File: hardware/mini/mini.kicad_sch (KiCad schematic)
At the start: 12 parts, among them J1 Conn_01x03, J2 Conn_02x05_Odd_Even, J3 Conn_02x05_Odd_Even

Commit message: route power stage
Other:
- sheet channel_A ports: added CONVERTER_~{INT}, SENSE_~{INT}; removed SENSE_INT
- sheet channel_B ports: added CONVERTER_~{INT}, SENSE_~{INT}; removed SENSE_INT
- sheet interface ports: added COL_2; removed ROW_3, ROW_4
- sheet mcu ports: added COL_2, CONVERTER_INT_A, CONVERTER_INT_B; removed ROW_3, ROW_4

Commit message: route
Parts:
- added N2: Breadboard, symbol Mechanical:Housing
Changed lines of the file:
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@@
+	)
+	(symbol
+		(lib_id "Mechanical:Housing")
+		(at 182.88 156.21 0)
+		(unit 1)
+		(exclude_from_sim no)
+		(in_bom yes)
+		(on_board yes)
+		(dnp no)
+		(fields_autoplaced yes)
+		(property "Reference" "N2"
+			(at 186.69 155.2574 0)
+			(effects
+				(font
+					(size 1.27 1.27)
+				)
+				(justify left)
+			)
+		)
+		(property "Value" "Breadboard"
+			(at 186.69 157.7974 0)
+			(effects
+				(font
+					(size 1.27 1.27)
+				)
+				(justify left)
+			)
+		)
+		(property "Footprint" ""
+			(at 184.15 154.94 0)
+			(effects
+				(font
+					(size 1.27 1.27)
+				)
+				(hide yes)
+			)
+		)
+		(property "Datasheet" "~"
+			(at 184.15 154.94 0)
+			(effects
+				(font
+					(size 1.27 1.27)
+				)
+				(hide yes)
+			)
+		)
+		(property "Description" "Housing"
+			(at 182.88 156.21 0)
+			(effects
+				(font
+					(size 1.27 1.27)
+				)
+				(hide yes)
+			)
+		)
+		(instances
+			(project ""
+				(path "/5aaaac9a-5acd-4aef-ad51-a6d04aa88705"
+					(reference "N2")
+					(unit 1)
+				)
+			)
+		)
 	)
 	(symbol

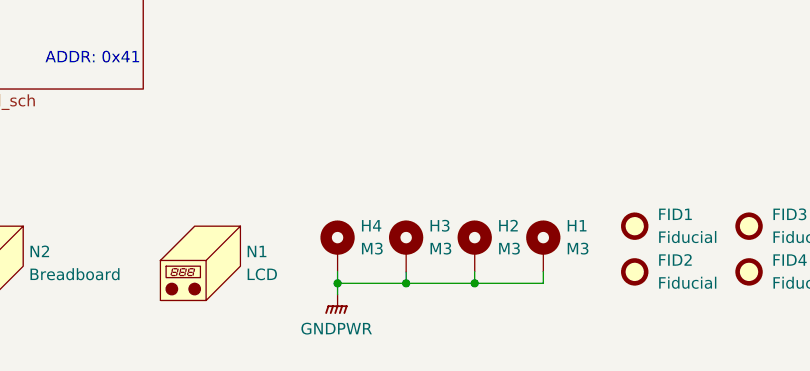
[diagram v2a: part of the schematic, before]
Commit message: route digitals
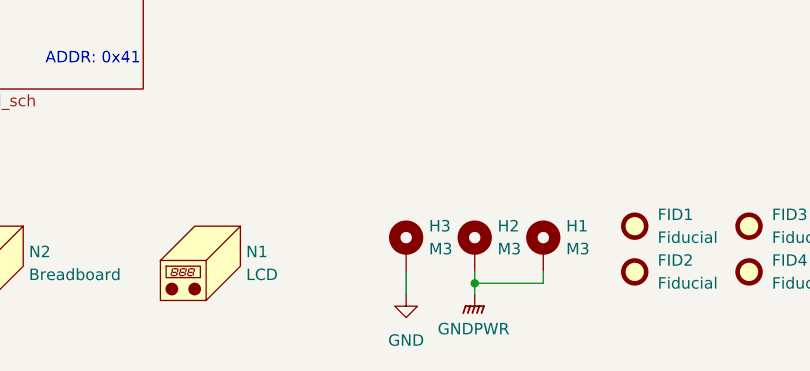
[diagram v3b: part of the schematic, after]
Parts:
- removed H4: M3, MountingHole:MountingHole_3.2mm_M3_DIN965_Pad_TopBottom, symbol Mechanical:MountingHole_Pad
- N2: footprint (none) -> protovolt_mini_fp:Breadboard_400P
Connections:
- net GND: now also H3.1
- net GNDPWR: no longer H3.1

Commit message: reroute all except 3V3 & GND
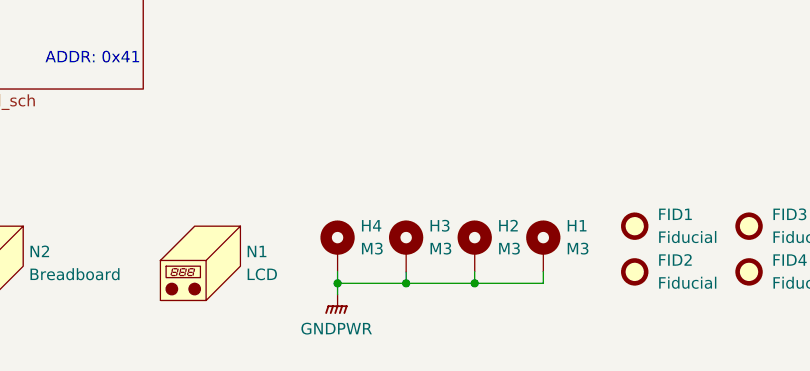
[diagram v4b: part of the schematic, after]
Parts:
- added H4: M3, MountingHole:MountingHole_3.2mm_M3_DIN965_Pad_TopBottom, symbol Mechanical:MountingHole_Pad
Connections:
- net GND: no longer H3.1
- net GNDPWR: now also H3.1, H4.1
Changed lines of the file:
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@@
+	)
+	(junction
+		(at 220.98 158.75)
+		(diameter 0)
+		(color 0 0 0 0)
 	)
 	(junction
@@
 	)
 	(junction
+		(at 228.6 158.75)
+		(diameter 0)
+		(color 0 0 0 0)
+	)
+	(junction
 		(at 236.22 55.88)
 		(diameter 0)
@@
 	(wire
 		(pts
-			(xy 228.6 157.48) (xy 228.6 160.02)
-		)
-		(stroke
-			(width 0)
-			(type default)
-		)
-	)
-	(wire
-		(pts
-			(xy 236.22 158.75) (xy 236.22 160.02)
+			(xy 220.98 158.75) (xy 220.98 160.02)
 		)
 		(stroke
@@
 	(wire
 		(pts
+			(xy 228.6 157.48) (xy 228.6 158.75)
+		)
+		(stroke
+			(width 0)
+			(type default)
+		)
+	)
+	(wire
+		(pts
+			(xy 220.98 158.75) (xy 228.6 158.75)
+		)
+		(stroke
+			(width 0)
+			(type default)
+		)
+	)
+	(wire
+		(pts
 			(xy 168.91 125.73) (xy 152.4 125.73)
 		)
@@
 	(wire
 		(pts
+			(xy 220.98 157.48) (xy 220.98 158.75)
+		)
+		(stroke
+			(width 0)
+			(type default)
+		)
+	)
+	(wire
+		(pts
 			(xy 90.17 49.53) (xy 102.87 49.53)
 		)
@@
 		(pts
 			(xy 90.17 63.5) (xy 96.52 63.5)
+		)
+		(stroke
+			(width 0)
+			(type default)
+		)
+	)
+	(wire
+		(pts
+			(xy 228.6 158.75) (xy 236.22 158.75)
 		)
 		(stroke
@@
 	(symbol
 		(lib_id "Mechanical:MountingHole_Pad")
+		(at 220.98 154.94 0)
+		(unit 1)
+		(exclude_from_sim no)
+		(in_bom no)
+		(on_board yes)
+		(dnp no)
+		(fields_autoplaced yes)
+		(property "Reference" "H4"
+			(at 223.52 152.3999 0)
+			(effects
+				(font
+					(size 1.27 1.27)
+				)
+				(justify left)
+			)
+		)
+		(property "Value" "M3"
+			(at 223.52 154.9399 0)
+			(effects
+				(font
+					(size 1.27 1.27)
+				)
+				(justify left)
+			)
+		)
+		(property "Footprint" "MountingHole:MountingHole_3.2mm_M3_DIN965_Pad_TopBottom"
+			(at 220.98 154.94 0)
+			(effects
+				(font
+					(size 1.27 1.27)
+				)
+				(hide yes)
+			)
+		)
+		(property "Datasheet" "~"
+			(at 220.98 154.94 0)
+			(effects
+				(font
+					(size 1.27 1.27)
+				)
+				(hide yes)
+			)
+		)
+		(property "Description" "Mounting Hole with connection"
+			(at 220.98 154.94 0)
+			(effects
+				(font
+					(size 1.27 1.27)
+				)
+				(hide yes)
+			)
+		)
+		(pin "1"
+		)
+		(instances
+			(project "mini"
+				(path "/5aaaac9a-5acd-4aef-ad51-a6d04aa88705"
+					(reference "H4")
+					(unit 1)
+				)
+			)
+		)
+	)
+	(symbol
+		(lib_id "Mechanical:MountingHole_Pad")
 		(at 236.22 154.94 0)
 		(unit 1)
@@
 	(symbol
 		(lib_id "power:GNDPWR")
-		(at 236.22 160.02 0)
+		(at 220.98 160.02 0)
 		(unit 1)
 		(exclude_from_sim no)
@@
 		(fields_autoplaced yes)
 		(property "Reference" "#PWR0123"
-			(at 236.22 165.1 0)
+			(at 220.98 165.1 0)
 			(effects
 				(font
@@
 		)
 		(property "Value" "GNDPWR"
-			(at 236.093 163.83 0)
+			(at 220.853 163.83 0)
 			(effects
 				(font
@@
 		)
 		(property "Footprint" ""
-			(at 236.22 161.29 0)
+			(at 220.98 161.29 0)
 			(effects
 				(font
@@
 		)
 		(property "Datasheet" ""
-			(at 236.22 161.29 0)
+			(at 220.98 161.29 0)
 			(effects
 				(font
@@
 		)
 		(property "Description" "Power symbol creates a global label with name \"GNDPWR\" , global ground"
-			(at 236.22 160.02 0)
+			(at 220.98 160.02 0)
 			(effects
 				(font
@@
 					(unit 1)
 				)
-			)
-		)
-	)
-	(symbol
-		(lib_id "power:GND")
-		(at 228.6 160.02 0)
-		(unit 1)
-		(exclude_from_sim no)
-		(in_bom yes)
-		(on_board yes)
-		(dnp no)
-		(fields_autoplaced yes)
-		(property "Reference" "#PWR057"
-			(at 228.6 166.37 0)
-			(effects
-				(font
-					(size 1.27 1.27)
-				)
-				(hide yes)
-			)
-		)
-		(property "Value" "GND"
-			(at 228.6 165.1 0)
-			(effects
-				(font
-					(size 1.27 1.27)
-				)
-			)
-		)
-		(property "Footprint" ""
-			(at 228.6 160.02 0)
-			(effects
-				(font
-					(size 1.27 1.27)
-				)
-				(hide yes)
-			)
-		)
-		(property "Datasheet" ""
-			(at 228.6 160.02 0)
-			(effects
-				(font
-					(size 1.27 1.27)
-				)
-				(hide yes)
-			)
-		)
-		(property "Description" "Power symbol creates a global label with name \"GND\" , ground"
-			(at 228.6 160.02 0)
-			(effects
-				(font
-					(size 1.27 1.27)
-				)
-				(hide yes)
-			)
-		)
-		(pin "1"
-		)
-		(instances
-			(project ""
-				(path "/5aaaac9a-5acd-4aef-ad51-a6d04aa88705"
-					(reference "#PWR057")
-					(unit 1)
-				)

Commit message: finish routing
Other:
- sheet channel_A ports: added GNDA; removed none
- sheet channel_B ports: added GNDA; removed none
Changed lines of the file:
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@@
+	(wire
+		(pts
+			(xy 201.93 86.36) (xy 201.93 88.9)
+		)
+		(stroke
+			(width 0)
+			(type default)
+		)
+	)
 	(wire
 		(pts
@@
 	(wire
 		(pts
+			(xy 199.39 135.89) (xy 201.93 135.89)
+		)
+		(stroke
+			(width 0)
+			(type default)
+		)
+	)
+	(wire
+		(pts
 			(xy 90.17 69.85) (xy 102.87 69.85)
 		)
@@
 	(wire
 		(pts
+			(xy 201.93 135.89) (xy 201.93 138.43)
+		)
+		(stroke
+			(width 0)
+			(type default)
+		)
+	)
+	(wire
+		(pts
 			(xy 236.22 50.8) (xy 236.22 53.34)
 		)
@@
 		(pts
 			(xy 168.91 128.27) (xy 151.13 128.27)
+		)
+		(stroke
+			(width 0)
+			(type default)
+		)
+	)
+	(wire
+		(pts
+			(xy 199.39 86.36) (xy 201.93 86.36)
 		)
 		(stroke
@@
 	)
 	(symbol
+		(lib_id "power:GND2")
+		(at 201.93 138.43 0)
+		(unit 1)
+		(exclude_from_sim no)
+		(in_bom yes)
+		(on_board yes)
+		(dnp no)
+		(fields_autoplaced yes)
+		(property "Reference" "#PWR013"
+			(at 201.93 144.78 0)
+			(effects
+				(font
+					(size 1.27 1.27)
+				)
+				(hide yes)
+			)
+		)
+		(property "Value" "GND2"
+			(at 201.93 143.51 0)
+			(effects
+				(font
+					(size 1.27 1.27)
+				)
+			)
+		)
+		(property "Footprint" ""
+			(at 201.93 138.43 0)
+			(effects
+				(font
+					(size 1.27 1.27)
+				)
+				(hide yes)
+			)
+		)
+		(property "Datasheet" ""
+			(at 201.93 138.43 0)
+			(effects
+				(font
+					(size 1.27 1.27)
+				)
+				(hide yes)
+			)
+		)
+		(property "Description" "Power symbol creates a global label with name \"GND2\" , ground"
+			(at 201.93 138.43 0)
+			(effects
+				(font
+					(size 1.27 1.27)
+				)
+				(hide yes)
+			)
+		)
+		(pin "1"
+		)
+		(instances
+			(project ""
+				(path "/5aaaac9a-5acd-4aef-ad51-a6d04aa88705"
+					(reference "#PWR013")
+					(unit 1)
+				)
+			)
+		)
+	)
+	(symbol
 		(lib_id "power:GNDPWR")
 		(at 236.22 113.03 0)
@@
 				(path "/5aaaac9a-5acd-4aef-ad51-a6d04aa88705"
 					(reference "#PWR07")
+					(unit 1)
+				)
+			)
+		)
+	)
+	(symbol
+		(lib_id "power:GND2")
+		(at 166.37 121.92 270)
+		(unit 1)
+		(exclude_from_sim no)
+		(in_bom yes)
+		(on_board yes)
+		(dnp no)
+		(fields_autoplaced yes)
+		(property "Reference" "#PWR04"
+			(at 160.02 121.92 0)
+			(effects
+				(font
+					(size 1.27 1.27)
+				)
+				(hide yes)
+			)
+		)
+		(property "Value" "GND2"
+			(at 162.56 121.9199 90)
+			(effects
+				(font
+					(size 1.27 1.27)
+				)
+				(justify right)
+			)
+		)
+		(property "Footprint" ""
+			(at 166.37 121.92 0)
+			(effects
+				(font
+					(size 1.27 1.27)
+				)
+				(hide yes)
+			)
+		)
+		(property "Datasheet" ""
+			(at 166.37 121.92 0)
+			(effects
+				(font
+					(size 1.27 1.27)
+				)
+				(hide yes)
+			)
+		)
+		(property "Description" "Power symbol creates a global label with name \"GND2\" , ground"
+			(at 166.37 121.92 0)
+			(effects
+				(font
+					(size 1.27 1.27)
+				)
+				(hide yes)
+			)
+		)
+		(pin "1"
+		)
+		(instances
+			(project "mini"
+				(path "/5aaaac9a-5acd-4aef-ad51-a6d04aa88705"
+					(reference "#PWR04")
 					(unit 1)
 				)
@@
 	)
 	(symbol
+		(lib_id "power:GND1")
+		(at 201.93 88.9 0)
+		(unit 1)
+		(exclude_from_sim no)
+		(in_bom yes)
+		(on_board yes)
+		(dnp no)
+		(fields_autoplaced yes)
+		(property "Reference" "#PWR010"
+			(at 201.93 95.25 0)
+			(effects
+				(font
+					(size 1.27 1.27)
+				)
+				(hide yes)
+			)
+		)
+		(property "Value" "GND1"
+			(at 201.93 93.98 0)
+			(effects
+				(font
+					(size 1.27 1.27)
+				)
+			)
+		)
+		(property "Footprint" ""
+			(at 201.93 88.9 0)
+			(effects
+				(font
+					(size 1.27 1.27)
+				)
+				(hide yes)
+			)
+		)
+		(property "Datasheet" ""
+			(at 201.93 88.9 0)
+			(effects
+				(font
+					(size 1.27 1.27)
+				)
+				(hide yes)
+			)
+		)
+		(property "Description" "Power symbol creates a global label with name \"GND1\" , ground"
+			(at 201.93 88.9 0)
+			(effects
+				(font
+					(size 1.27 1.27)
+				)
+				(hide yes)
+			)
+		)
+		(pin "1"
+		)
+		(instances
+			(project ""
+				(path "/5aaaac9a-5acd-4aef-ad51-a6d04aa88705"
+					(reference "#PWR010")
+					(unit 1)
+				)
+			)
+		)
+	)
+	(symbol
 		(lib_id "Mechanical:MountingHole_Pad")
 		(at 243.84 154.94 0)
@@
 				(path "/5aaaac9a-5acd-4aef-ad51-a6d04aa88705"
 					(reference "#PWR0123")
-					(unit 1)
-				)
-			)
-		)
-	)
-	(symbol
-		(lib_id "power:GND")
-		(at 166.37 121.92 270)
-		(mirror x)
-		(unit 1)
-		(exclude_from_sim no)
-		(in_bom yes)
-		(on_board yes)
-		(dnp no)
-		(property "Reference" "#PWR04"
-			(at 160.02 121.92 0)
-			(effects
-				(font
-					(size 1.27 1.27)
-				)
-				(hide yes)
-			)
-		)
-		(property "Value" "GND"
-			(at 162.56 121.9199 90)
-			(effects
-				(font
-					(size 1.27 1.27)
-				)
-				(justify right)
-			)
-		)
-		(property "Footprint" ""
-			(at 166.37 121.92 0)
-			(effects
-				(font
-					(size 1.27 1.27)
-				)
-				(hide yes)
-			)
-		)
-		(property "Datasheet" ""
-			(at 166.37 121.92 0)
-			(effects
-				(font
-					(size 1.27 1.27)
-				)
-				(hide yes)
-			)
-		)
-		(property "Description" "Power symbol creates a global label with name \"GND\" , ground"
-			(at 166.37 121.92 0)
-			(effects
-				(font
-					(size 1.27 1.27)
-				)
-				(hide yes)
-			)
-		)
-		(pin "1"
-		)
-		(instances
-			(project "mini"
-				(path "/5aaaac9a-5acd-4aef-ad51-a6d04aa88705"
-					(reference "#PWR04")
 					(unit 1)
 				)
@@
 			)
 		)
+		(pin "GNDA" input
+			(at 199.39 86.36 0)
+			(effects
+				(font
+					(size 1.27 1.27)
+				)
+				(justify right)
+			)
+		)
 		(instances
 			(project "mini"
@@
 			)
 		)
+		(pin "GNDA" input
+			(at 199.39 135.89 0)
+			(effects
+				(font
+					(size 1.27 1.27)
+				)
+				(justify right)
+			)
+		)

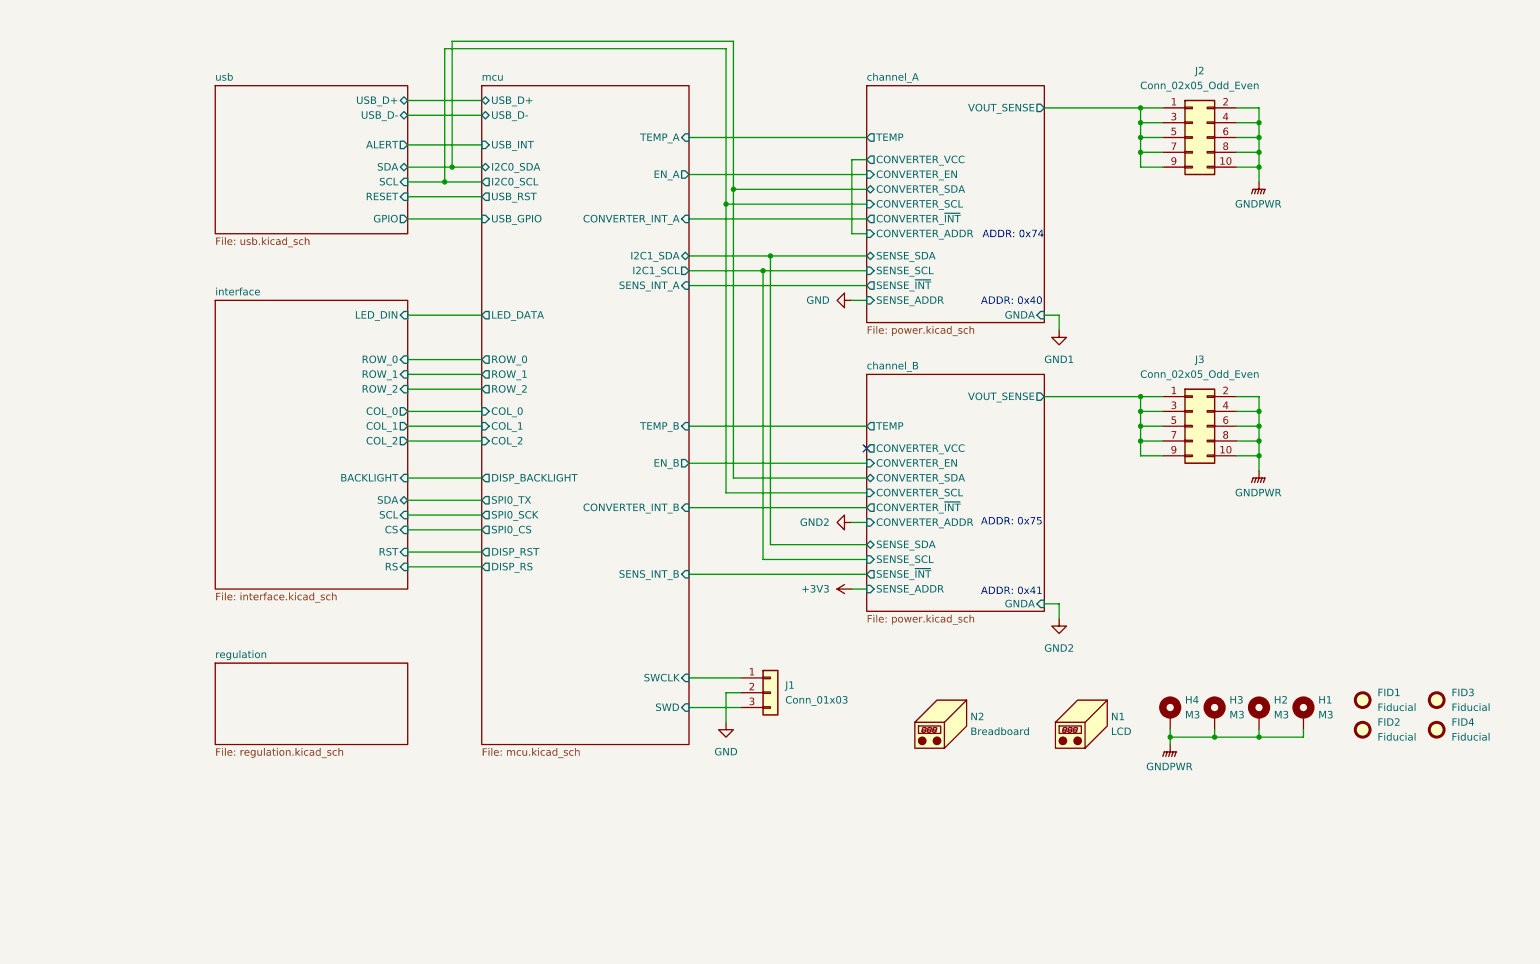
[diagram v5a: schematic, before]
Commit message: all DRC except silkscreen warnings
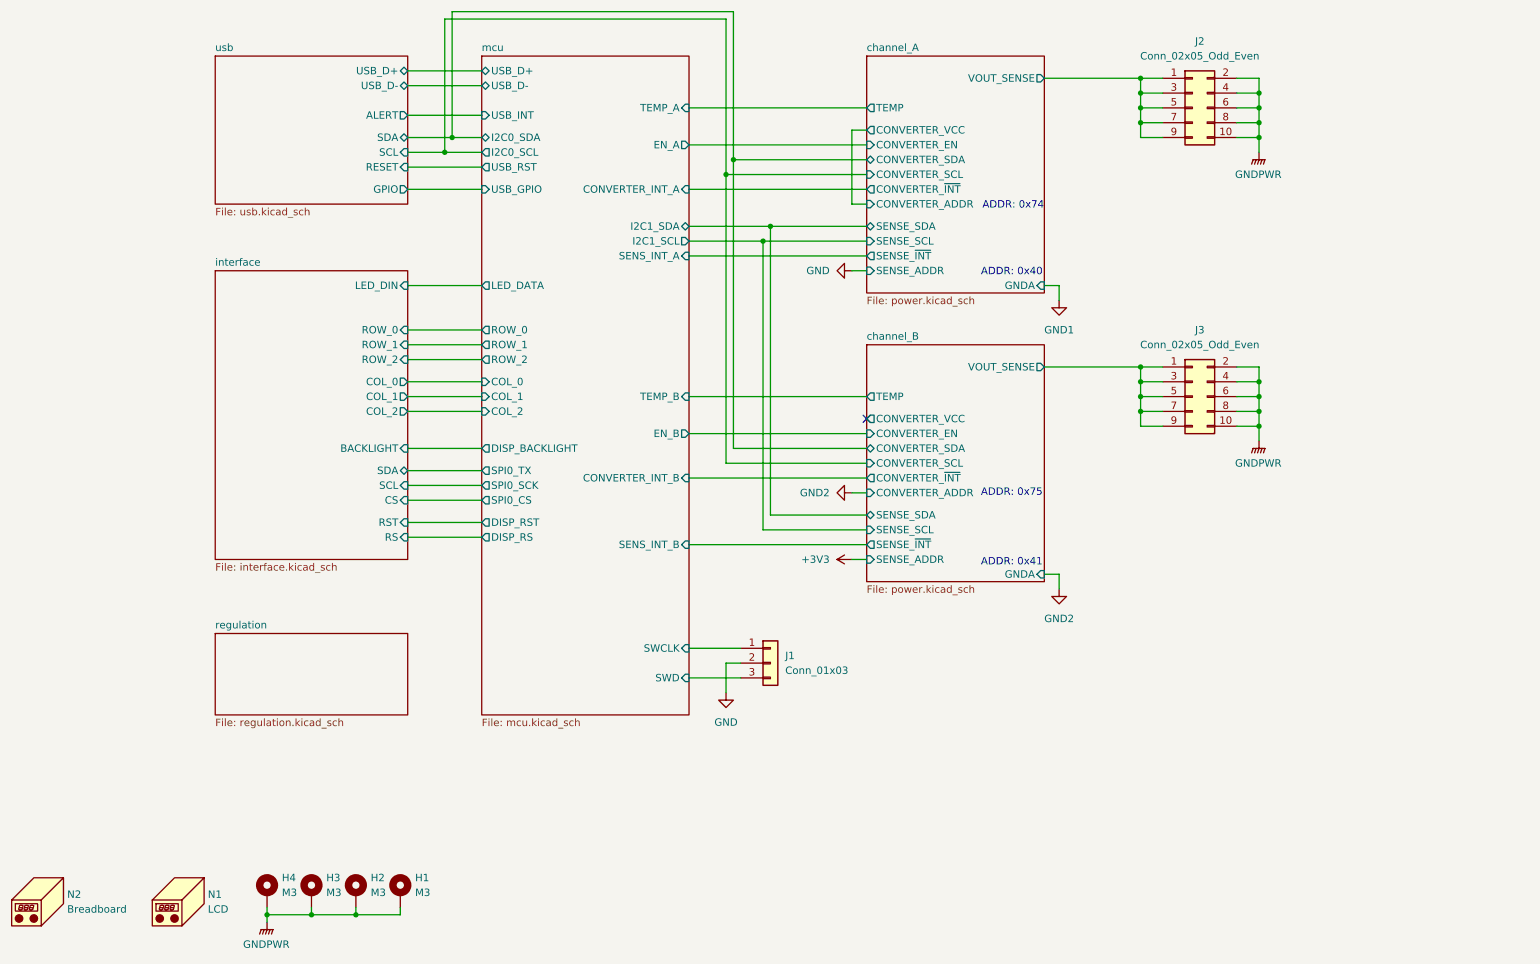
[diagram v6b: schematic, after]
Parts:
- removed FID1, FID2, FID3, FID4: Fiducial, Fiducial:Fiducial_1mm_Mask2mm, symbol Mechanical:Fiducial
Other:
- moved on the sheet: H1, H2, H3, H4, J1, J2, J3, N1, N2
